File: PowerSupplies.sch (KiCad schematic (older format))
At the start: 44 parts, among them Q301 BC847B-13-F, Q302 BC856B-13-F, Q305 TK32A12N1,S4X, Q306 TK32A12N1,S4X, U301 FDA217, U302 LTC7138EMSE-PBF, U303 TPS560200, U304 TLV70430_SOT23-5, U305 REF2925AIDBZT, U306 TPS560200

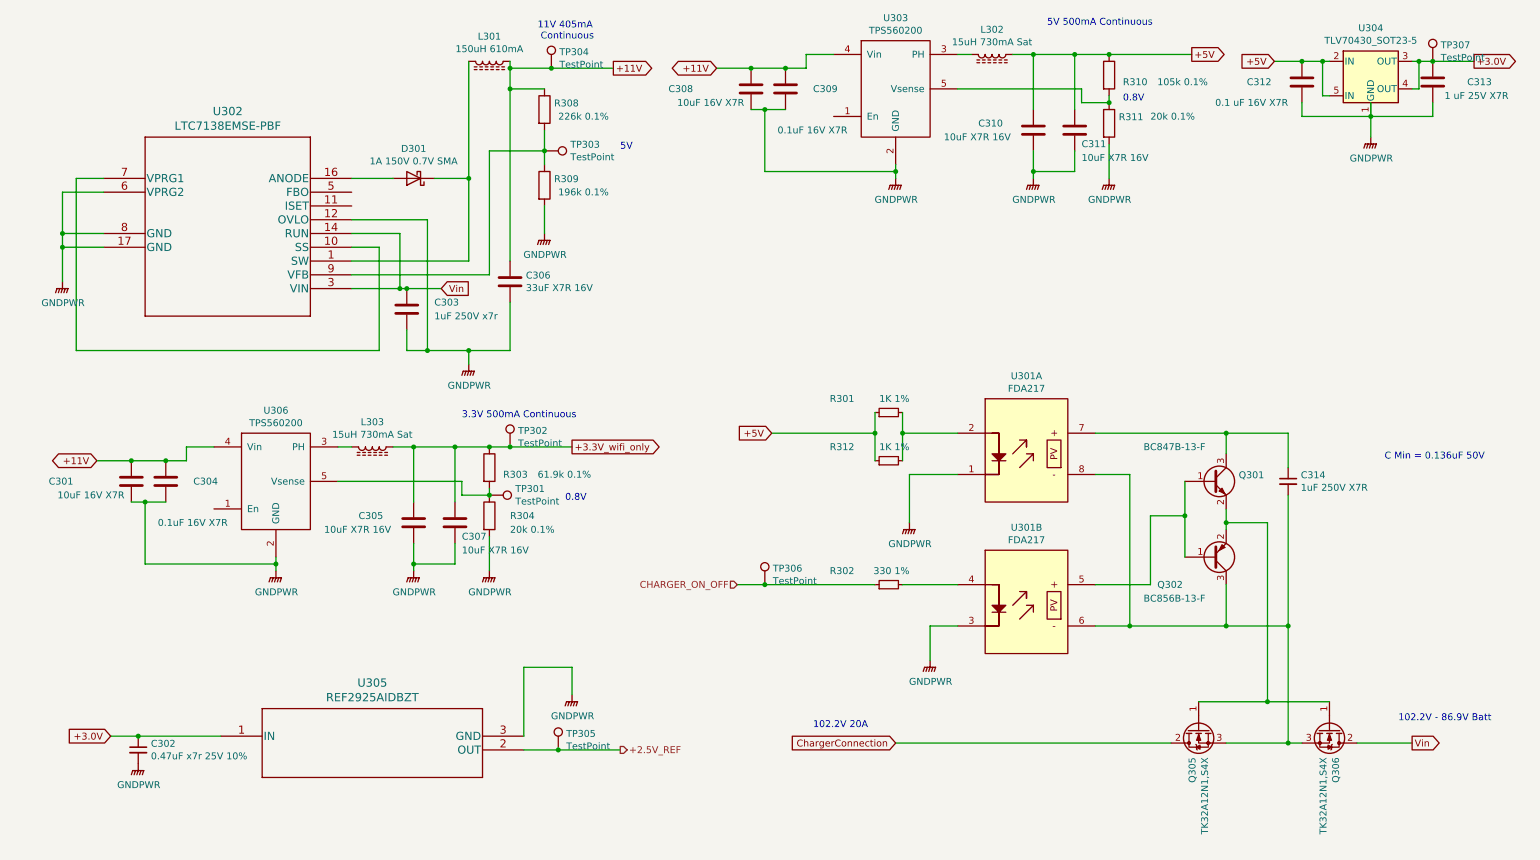
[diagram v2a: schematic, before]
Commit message: Consolidated a lot of part values that were the same part but not detected the same by Boms_away BOM editor because of subtle differences in how I specified the values. Added Digi-key part numbers to the resistors. Replaced 2mOhm .5W current sense resistors with 1W 2mOhm Thin Film resistors (lower inductance than metal element), And fixed a bug where I was earthing the return feed of the Solar inverter before passing through the current sense resistor.
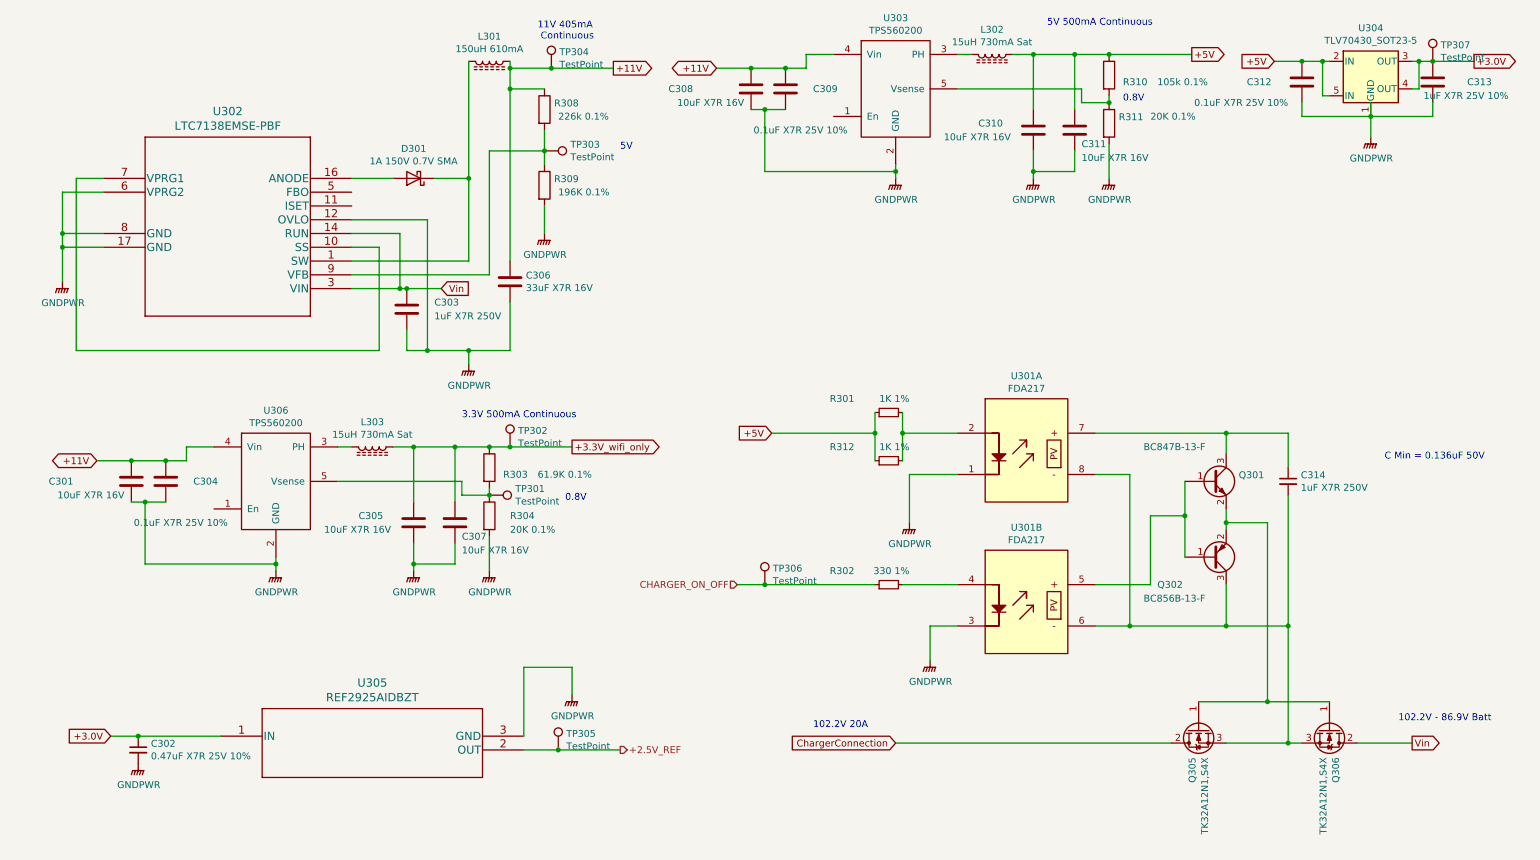
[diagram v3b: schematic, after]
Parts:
- C301, C308: value 10uF 16V X7R -> 10uF X7R 16V; MFR (none) -> -; MPN (none) -> -; SPN (none) -> -; SPR (none) -> -; SPURL (none) -> -
- C302: value 0.47uF x7r 25V 10% -> 0.47uF X7R 25V 10%; MFR (none) -> -; MPN (none) -> -; SPN (none) -> -; SPR (none) -> -; SPURL (none) -> -
- C303: value 1uF 250V x7r -> 1uF X7R 250V; MFR (none) -> -; MPN (none) -> -; SPN (none) -> -; SPR (none) -> -; SPURL (none) -> -
- C304, C309: value 0.1uF 16V X7R -> 0.1uF X7R 25V 10%; MFR (none) -> Samsung; MPN (none) -> CL21B104KACNNNC; SPN (none) -> 1276-1099-1-ND; SPR (none) -> digikey; SPURL (none) -> -
- C305, C306, C307, C310, C311, D301, L301, L302, L303, Q301, Q302, Q305, Q306, R302, TP301, TP302, TP303, TP304, TP305, TP306, TP307, U301, U302, U303, U304, U305, U306: MFR (none) -> -; MPN (none) -> -; SPN (none) -> -; SPR (none) -> -; SPURL (none) -> -
- C312: value 0.1 uF 16V X7R -> 0.1uF X7R 25V 10%; MFR (none) -> Samsung; MPN (none) -> CL21B104KACNNNC; SPN (none) -> 1276-1099-1-ND; SPR (none) -> digikey; SPURL (none) -> -
- C313: value 1 uF 25V X7R -> 1uF X7R 25V 10%; MFR (none) -> Wurth Elektronik; MPN (none) -> 885012207078; SPN (none) -> 732-7672-1-ND; SPR (none) -> digikey; SPURL (none) -> -
- C314: value 1uF 250V X7R -> 1uF X7R 250V; MFR (none) -> -; MPN (none) -> -; SPN (none) -> -; SPR (none) -> -; SPURL (none) -> -
- R301, R312: MFR (none) -> Yageo; MPN (none) -> RC0805FR-071KL; SPN (none) -> 311-1.00KCRCT-ND; SPR (none) -> digikey; SPURL (none) -> -
- R303: value 61.9k 0.1% -> 61.9K 0.1%; MFR (none) -> Panasonic Electronic Components; MPN (none) -> ERA-6AEB6192V; SPN (none) -> P61.9KDACT-ND; SPR (none) -> digikey; SPURL (none) -> -
- R304, R311: value 20k 0.1% -> 20K 0.1%; MFR (none) -> Panasonic Electronic Components; MPN (none) -> ERA-6AEB203V; SPN (none) -> P20KDACT-ND; SPR (none) -> digikey; SPURL (none) -> -
- R308: MFR (none) -> Panasonic Electronic Components; MPN (none) -> ERA-6AEB2263V; SPN (none) -> P226KDACT-ND; SPR (none) -> digikey; SPURL (none) -> -
- R309: value 196k 0.1% -> 196K 0.1%; MFR (none) -> Panasonic Electronic Components; MPN (none) -> ERA-6AEB1963V; SPN (none) -> P196KDACT-ND; SPR (none) -> digikey; SPURL (none) -> -
- R310: MFR (none) -> Panasonic Electronic Components; MPN (none) -> ERA-6AEB1053V; SPN (none) -> P105KDACT-ND; SPR (none) -> digikey; SPURL (none) -> -

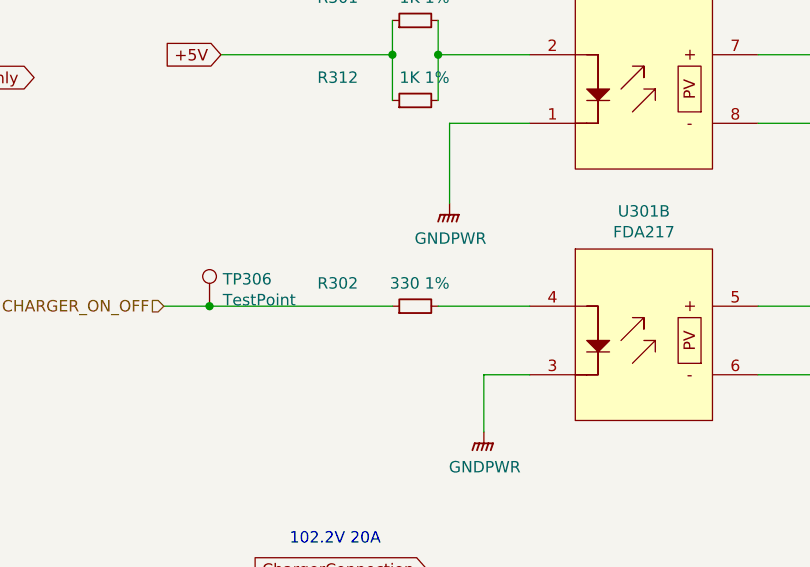
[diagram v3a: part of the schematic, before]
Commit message: change a few compoents foot prints for SOT23 to SOT23-Handsoldered, and SOT23-5 to SOT23-5-Handsoldered
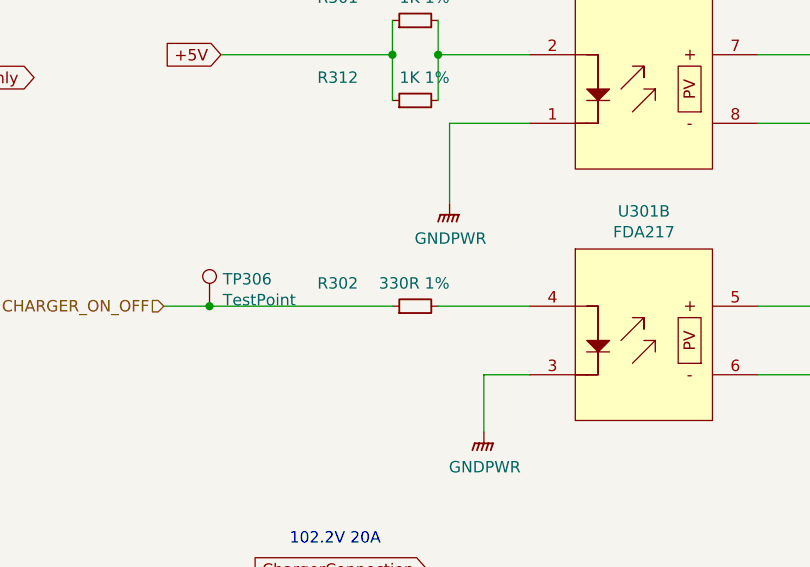
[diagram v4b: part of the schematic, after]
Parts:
- C302: MFR - -> Samsung Electro-Mechanics; MPN - -> CL21B474KAFNNNE; SPN - -> 1276-1074-1-ND; SPR - -> digikey
- C306: MFR - -> TDK Corporation; MPN - -> C4532X7R1C336M250KC; SPN - -> 445-3924-1-ND; SPR - -> digikey
- R302: value 330 1% -> 330R 1%; MFR - -> TE Connectivity Passive Product; MPN - -> CRGCQ0805F330R; SPN - -> A129743CT-ND; SPR - -> digikey
- U304: footprint Package_TO_SOT_SMD:SOT-23-5 -> Package_TO_SOT_SMD:SOT-23-5_HandSoldering
- U305: MFR - -> Texas Instruments; MPN - -> REF2925AIDBZT; SPN - -> 296-13482-1-ND; SPR - -> digikey

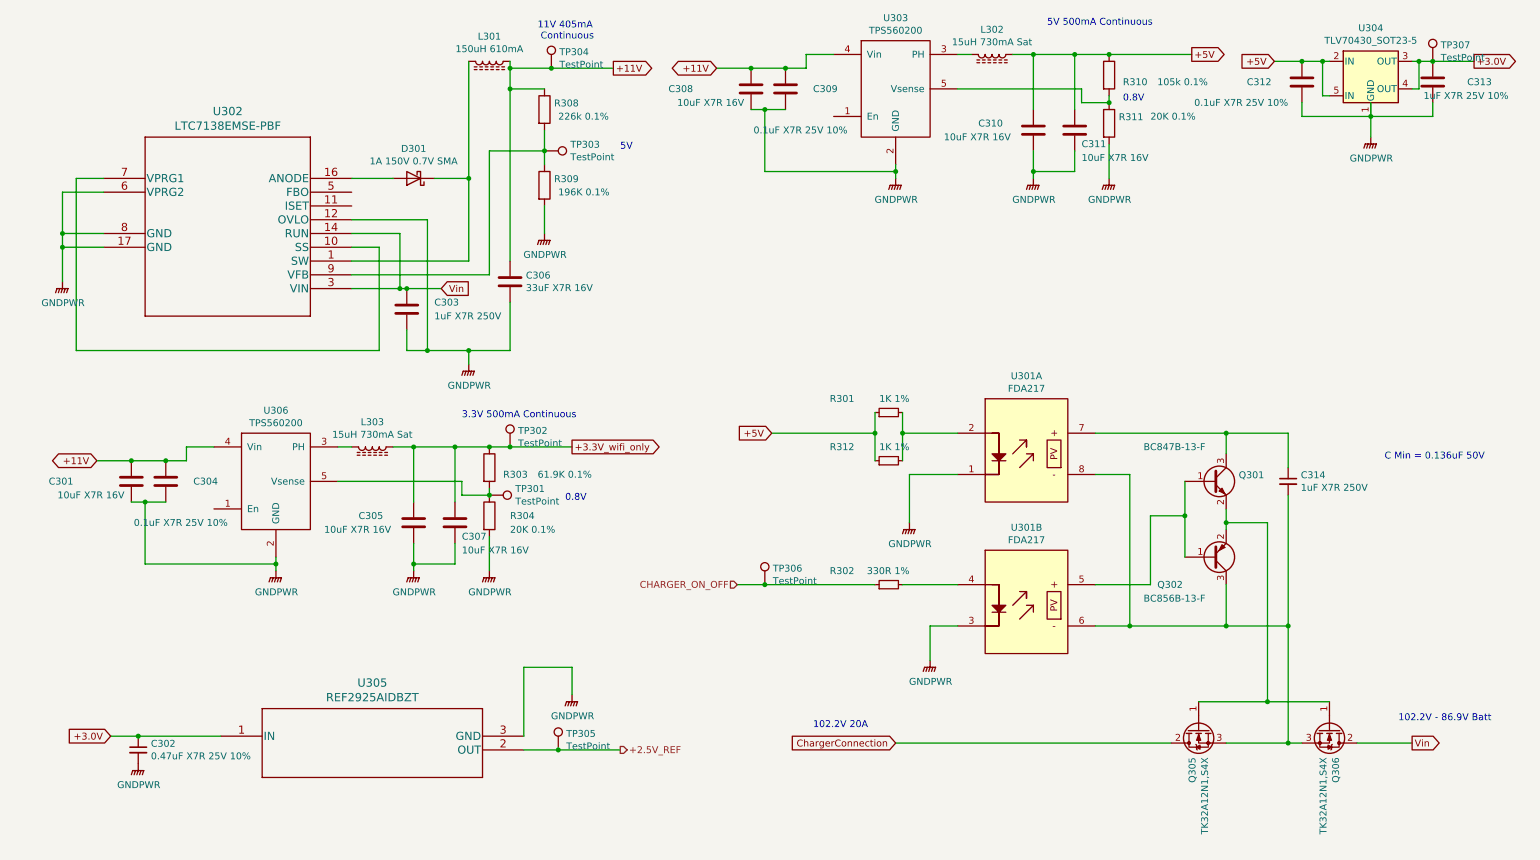
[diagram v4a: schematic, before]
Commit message: Finished adding digi key part numbers, for now git add *
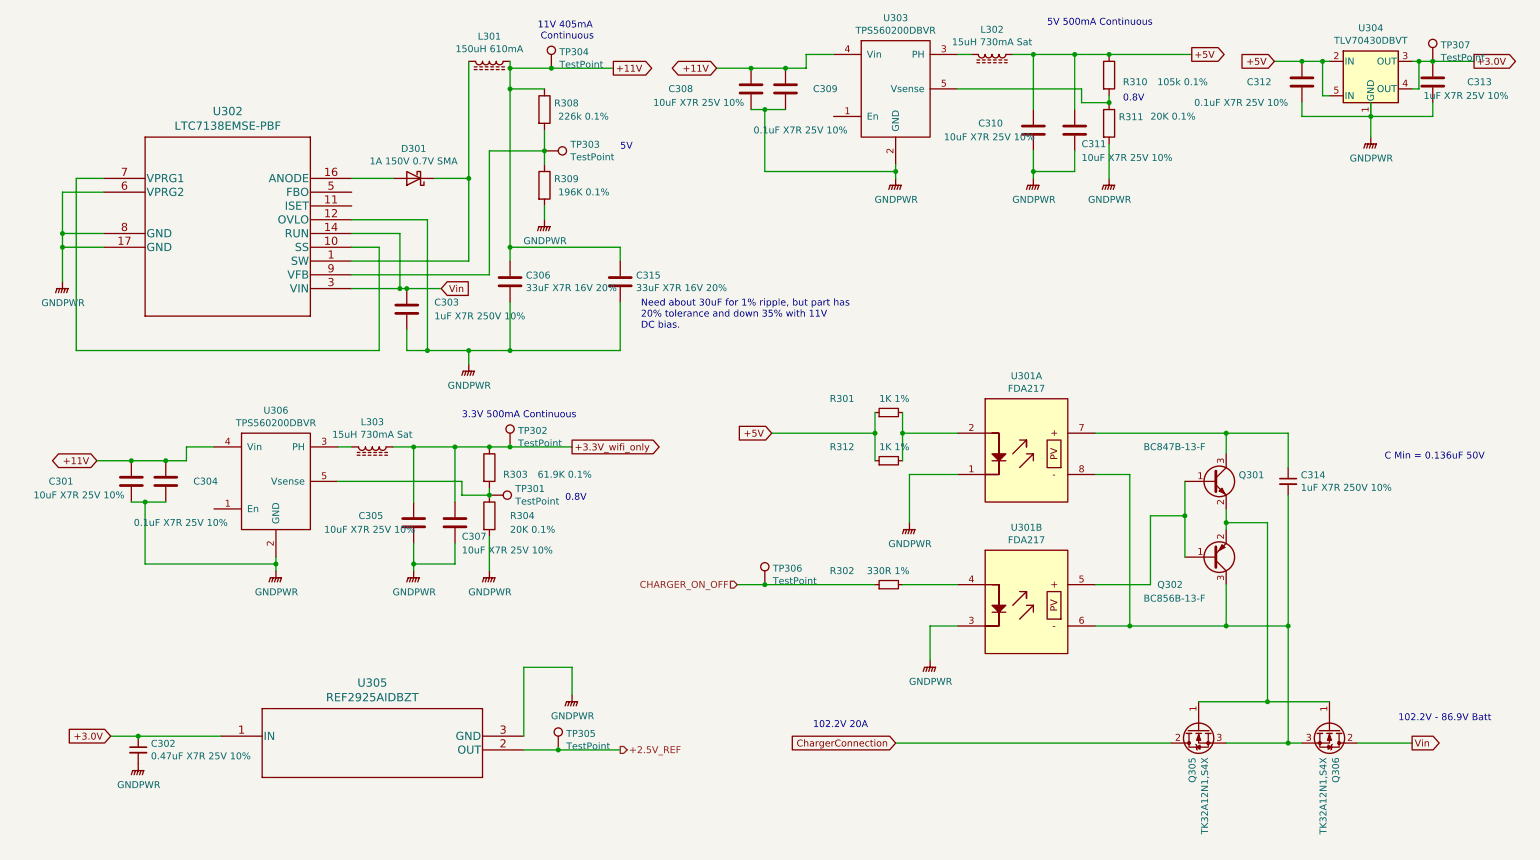
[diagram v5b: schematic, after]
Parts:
- added C315: 33uF X7R 16V 20%, Capacitors_SMD:C_1812_HandSoldering, symbol Device:C
- C301, C305, C307, C308, C310, C311: value 10uF X7R 16V -> 10uF X7R 25V 10%; MFR - -> Samsung Electro-Mechanics; MPN - -> CL31B106KAHNNNE; SPN - -> 1276-1804-1-ND; SPR - -> digikey
- C303, C314: value 1uF X7R 250V -> 1uF X7R 250V 10%; MFR - -> TDK Corporation; MPN - -> C5750X7R2E105K230KA; SPN - -> 445-2304-1-ND; SPR - -> digikey
- C306: value 33uF X7R 16V -> 33uF X7R 16V 20%
- D301: MFR - -> Diodes Incorporated; MPN - -> SBR1U150SA-13; SPN - -> SBR1U150SA-13DICT-ND; SPR - -> digikey
- L301: MFR - -> Bourns Inc.; MPN - -> PM3308-151M-RC; SPN - -> PM3308-151M-RCCT-ND; SPR - -> digikey
- L302, L303: MFR - -> Taiyo Yuden; MPN - -> CBC3225T150KR; SPN - -> 587-3066-1-ND; SPR - -> digikey
- Q301: MFR - -> Diodes Incorporated; MPN - -> BC847B-13-F; SPN - -> BC847B-13-FDICT-ND; SPR - -> digikey
- Q302: MFR - -> Diodes Incorporated; MPN - -> BC856B-13-F; SPN - -> BC856B-13-FDICT-ND; SPR - -> digikey
- Q305, Q306: MFR - -> Toshiba Semiconductor and Storage; MPN - -> TK32A12N1,S4X; SPN - -> TK32A12N1S4X-ND; SPR - -> digikey
- U301: MFR - -> IXYS Integrated Circuits Division; MPN - -> FDA217S; SPN - -> CLA408-ND; SPR - -> digikey
- U302: MFR - -> Linear Technology/Analog Devices; MPN - -> LTC7138EMSE#PBF; SPN - -> LTC7138EMSE#PBF-ND; SPR - -> digikey
- U303, U306: value TPS560200 -> TPS560200DBVR; MFR - -> Texas Instruments; MPN - -> TPS560200DBVR; SPN - -> 296-38559-1-ND; SPR - -> digikey
- U304: value TLV70430_SOT23-5 -> TLV70430DBVT; MFR - -> Texas Instruments; MPN - -> TLV70430DBVT; SPN - -> 296-32419-1-ND; SPR - -> digikey
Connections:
- net +11V: now also C315.1
- net GNDPWR: now also C315.2
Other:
- note added: "Need about 30uF for 1% ripple, but part has\n20% tolerance and down 35% with 11V\nDC bias."

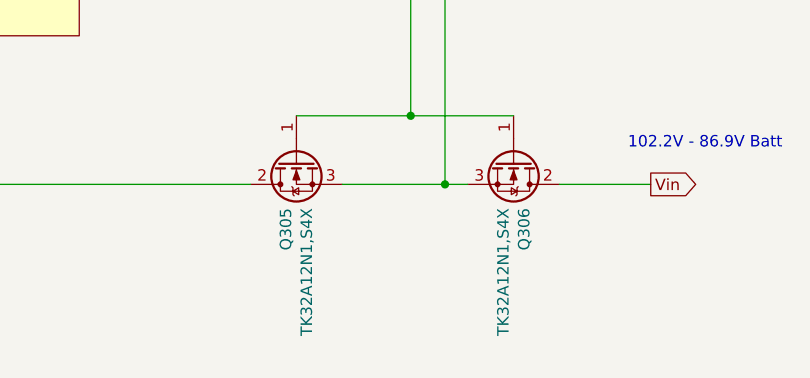
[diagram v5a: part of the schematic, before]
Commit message: added thermal via of .3 drill size and .6, I have read the recomenned size is .25 drill but the smallest JLCPCB do for double sided boards is .3
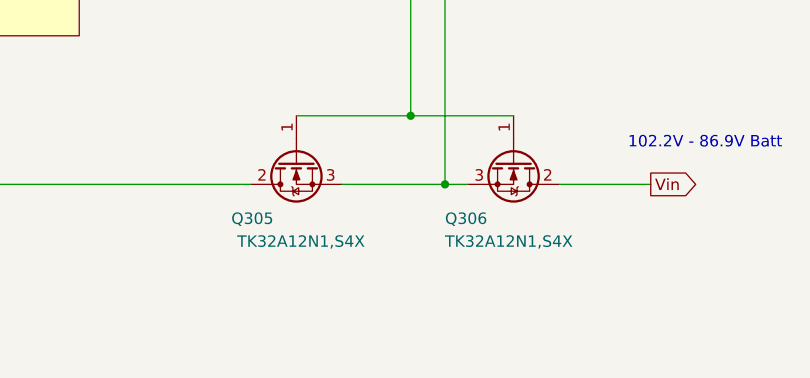
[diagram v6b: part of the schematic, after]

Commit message: Started making progress towards people being able to clone the the repository without getting messages about missing librarys needing rescue. started simplifying where some component librarys are located.
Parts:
- U302: symbol LT7138EMSEPBF:LTC7138EMSE-PBF -> AnalogDevices:LTC7138EMSE-PBF
